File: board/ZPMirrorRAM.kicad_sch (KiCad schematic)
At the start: 17 parts, among them IC1 74LS189, IC2 74LS189, IC3 74LS189, IC4 SN74LS189AN, U13 74F08, U24 74F20, U25 74F02, U26 74LS154, U27 74HC138

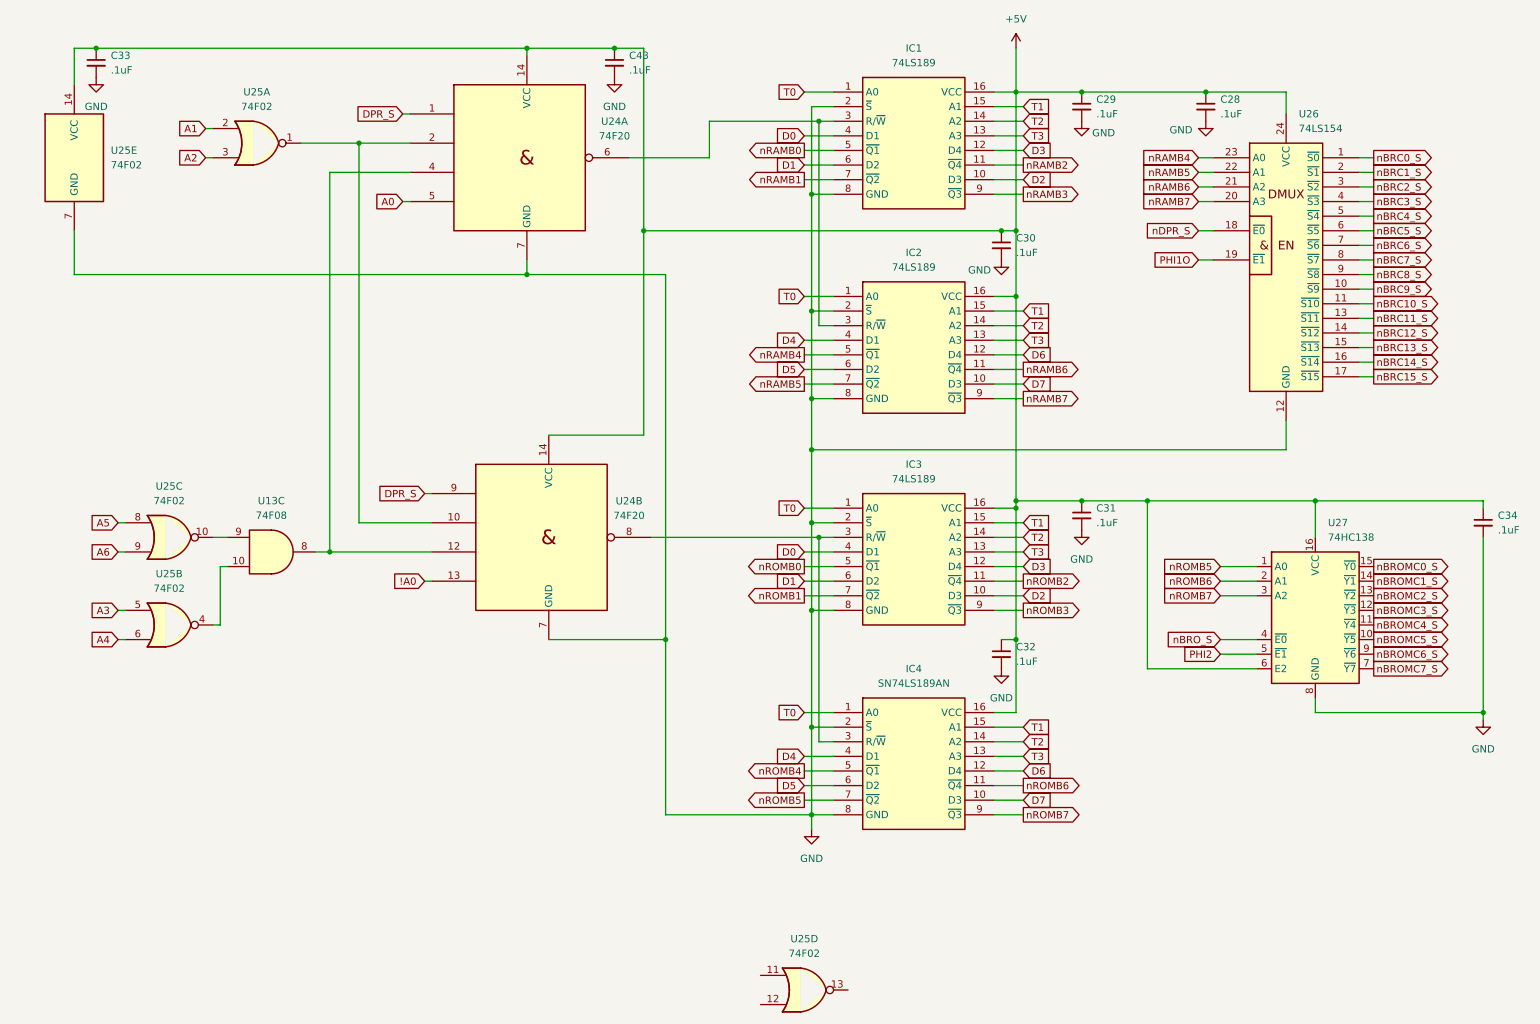
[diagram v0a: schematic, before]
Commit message: Fixing pin assignments
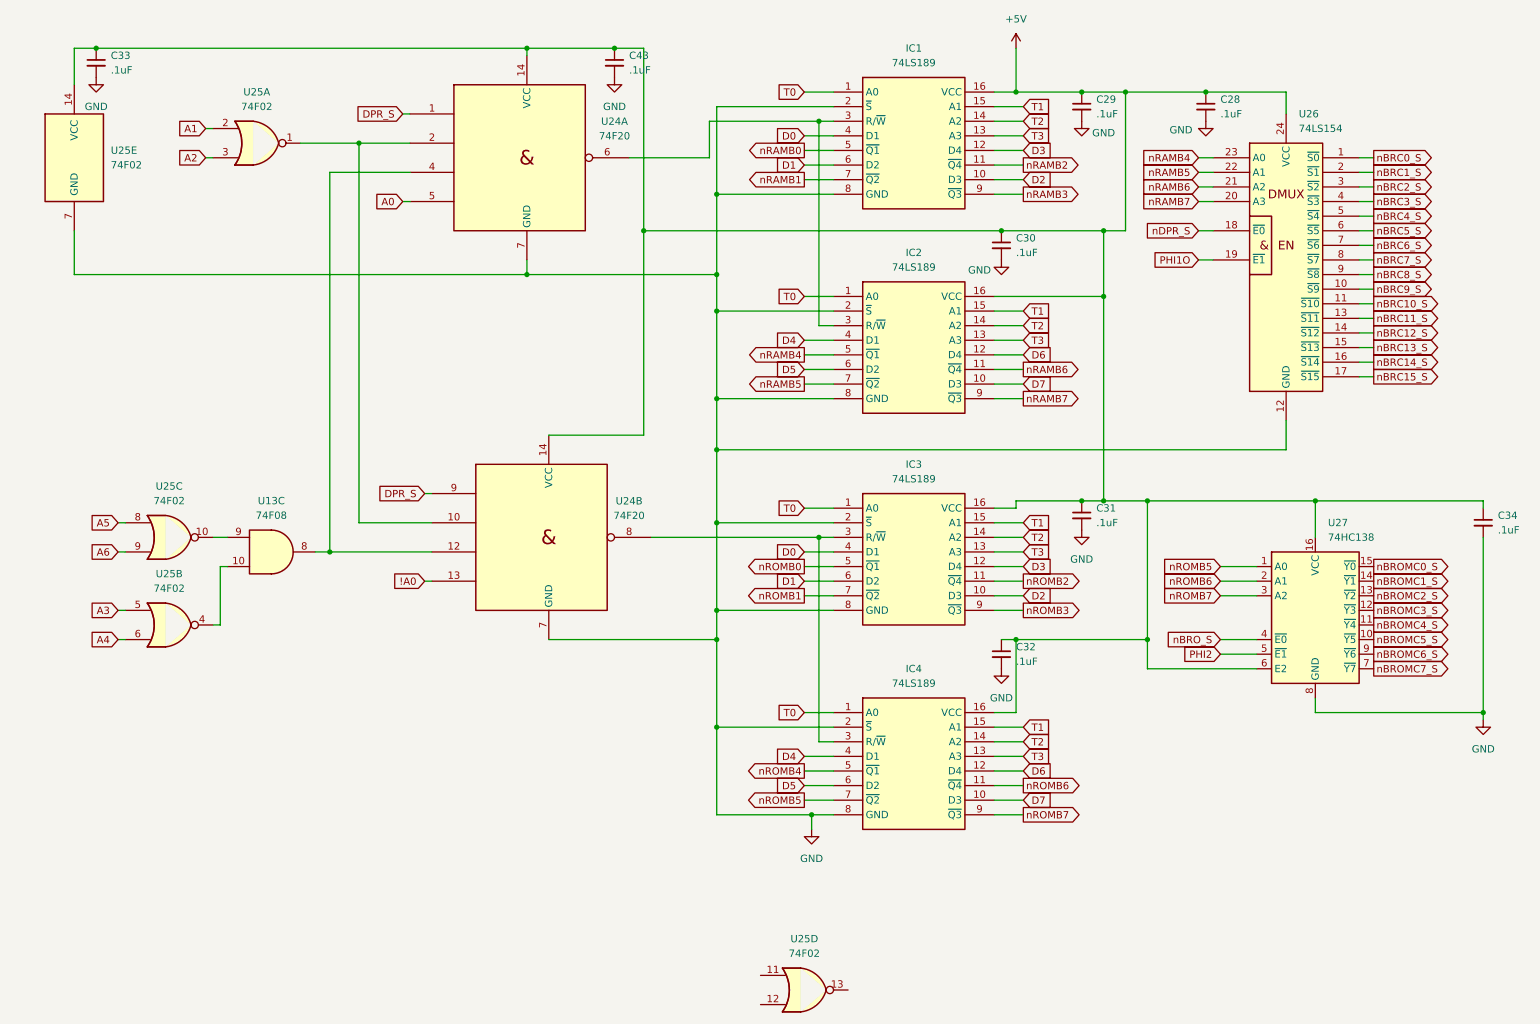
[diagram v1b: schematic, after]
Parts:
- IC4: value SN74LS189AN -> 74LS189

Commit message: Added surface mount version of memory daughter cards, and lots of schematic updates and fixes, including adding dedicated registers for shared memory bank select at $FFF1 and IRQ vTable entry selector at $FFF2 along with the IRQ vTable registers and priority encoders for 16 IRQs
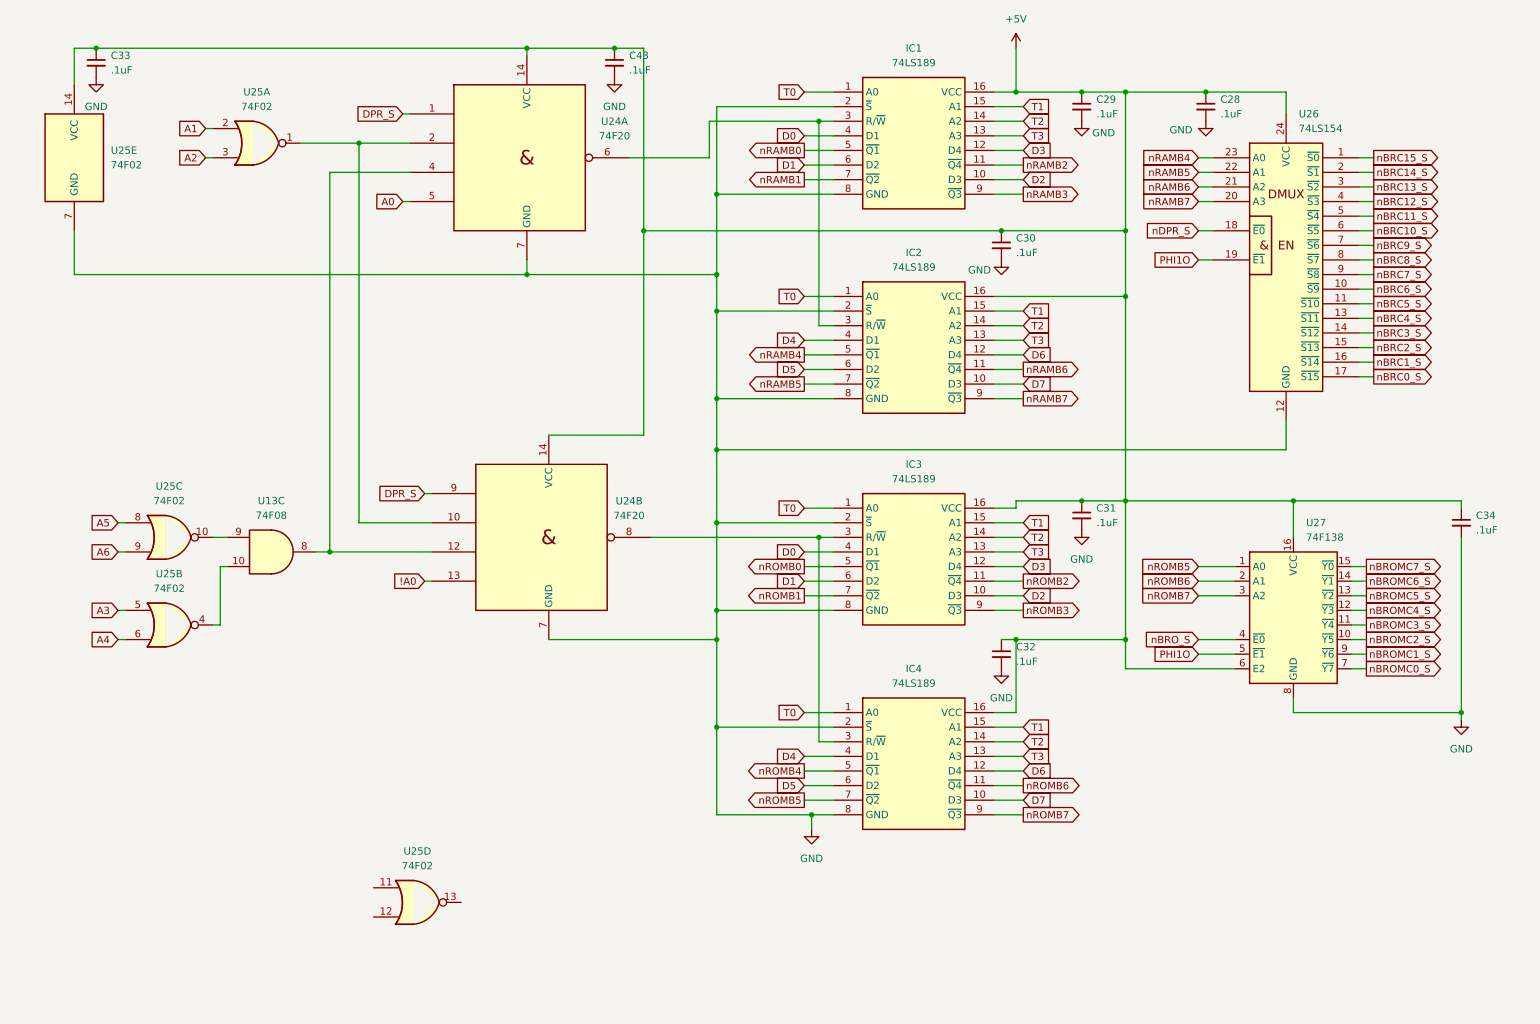
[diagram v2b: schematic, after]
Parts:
- U27: value 74HC138 -> 74F138
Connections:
- net PHI2 is gone; now on net PHI1O: U27.5 (~{E1})
- net nBRC0_S: now also U26.17 (~{S15}); no longer U26.1 (~{S0})
- net nBRC10_S: now also U26.6 (~{S5}); no longer U26.11 (~{S10})
- net nBRC11_S: now also U26.5 (~{S4}); no longer U26.13 (~{S11})
- net nBRC12_S: now also U26.4 (~{S3}); no longer U26.14 (~{S12})
- net nBRC13_S: now also U26.3 (~{S2}); no longer U26.15 (~{S13})
- net nBRC14_S: now also U26.2 (~{S1}); no longer U26.16 (~{S14})
- net nBRC15_S: now also U26.1 (~{S0}); no longer U26.17 (~{S15})
- net nBRC1_S: now also U26.16 (~{S14}); no longer U26.2 (~{S1})
- net nBRC2_S: now also U26.15 (~{S13}); no longer U26.3 (~{S2})
- net nBRC3_S: now also U26.14 (~{S12}); no longer U26.4 (~{S3})
- net nBRC4_S: now also U26.13 (~{S11}); no longer U26.5 (~{S4})
- net nBRC5_S: now also U26.11 (~{S10}); no longer U26.6 (~{S5})
- net nBRC6_S: now also U26.10 (~{S9}); no longer U26.7 (~{S6})
- net nBRC7_S: now also U26.9 (~{S8}); no longer U26.8 (~{S7})
- net nBRC8_S: now also U26.8 (~{S7}); no longer U26.9 (~{S8})
- net nBRC9_S: now also U26.7 (~{S6}); no longer U26.10 (~{S9})
- net nBROMC0_S: now also U27.7 (~{Y7}); no longer U27.15 (~{Y0})
- net nBROMC1_S: now also U27.9 (~{Y6}); no longer U27.14 (~{Y1})
- net nBROMC2_S: now also U27.10 (~{Y5}); no longer U27.13 (~{Y2})
- net nBROMC3_S: now also U27.11 (~{Y4}); no longer U27.12 (~{Y3})
- net nBROMC4_S: now also U27.12 (~{Y3}); no longer U27.11 (~{Y4})
- net nBROMC5_S: now also U27.13 (~{Y2}); no longer U27.10 (~{Y5})
- net nBROMC6_S: now also U27.14 (~{Y1}); no longer U27.9 (~{Y6})
- net nBROMC7_S: now also U27.15 (~{Y0}); no longer U27.7 (~{Y7})
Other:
- moved on the sheet: C34, U27

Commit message: More main PCB updates.  Rearranged some things.  Bypass caps near PS connector.  Moved front panel connector to opposite side of board.
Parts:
- IC1, IC2, IC3, IC4: footprint Package_DIP:DIP-16_W7.62mm_LongPads -> Package_DIP:DIP-16_W7.62mm_Socket_LongPads
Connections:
- net nDPR_S renamed nBRA_S
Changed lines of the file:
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@@
 		)
 	)
-	(global_label "nDPR_S"
+	(global_label "nBRA_S"
 		(shape input)
 		(at 223.52 52.07 180)
@@
 		)
 		(property "Intersheetrefs" "${INTERSHEET_REFS}"
-			(at 213.3987 52.07 0)
+			(at 213.5801 52.07 0)
 			(effects
 				(font
@@
 			)
 		)
-		(property "Footprint" "Package_DIP:DIP-16_W7.62mm_LongPads"
+		(property "Footprint" "Package_DIP:DIP-16_W7.62mm_Socket_LongPads"
 			(at 184.15 158.42 0)
 			(effects
@@
 			)
 		)
-		(property "Footprint" "Package_DIP:DIP-16_W7.62mm_LongPads"
+		(property "Footprint" "Package_DIP:DIP-16_W7.62mm_Socket_LongPads"
 			(at 184.15 122.86 0)
 			(effects
@@
 			)
 		)
-		(property "Footprint" "Package_DIP:DIP-16_W7.62mm_LongPads"
+		(property "Footprint" "Package_DIP:DIP-16_W7.62mm_Socket_LongPads"
 			(at 184.15 230.81 0)
 			(effects
@@
 			)
 		)
-		(property "Footprint" "Package_DIP:DIP-16_W7.62mm_LongPads"
+		(property "Footprint" "Package_DIP:DIP-16_W7.62mm_Socket_LongPads"
 			(at 184.15 195.25 0)
 			(effects

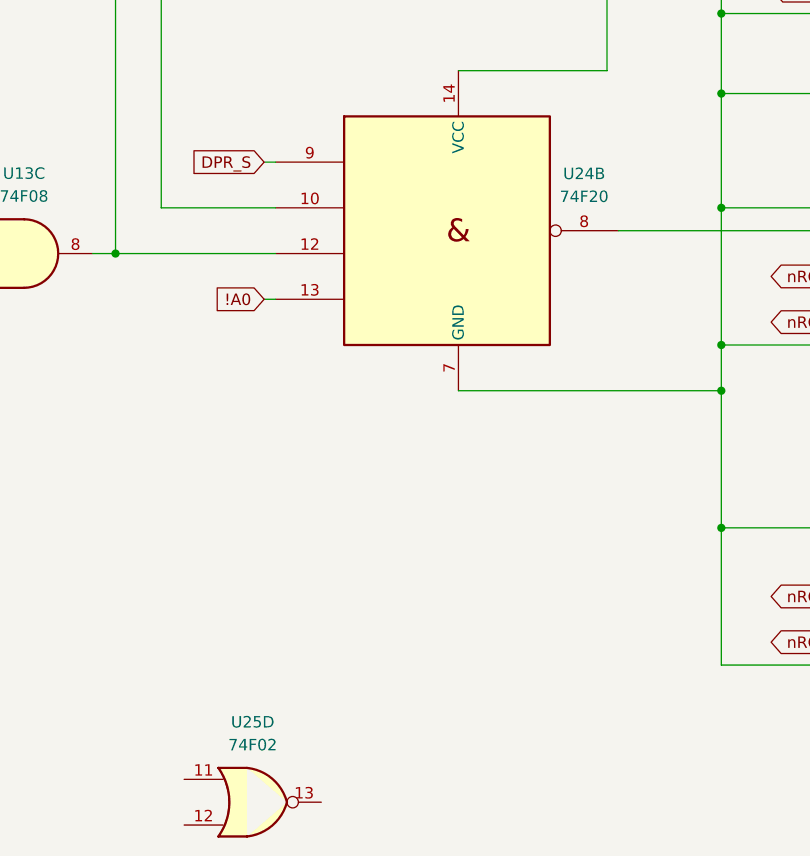
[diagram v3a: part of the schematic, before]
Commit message: Latest main PCB update with FFF1 and FFF2 added and decode logic updated to exclude FFFE and FFFF in nOSROM_S signal
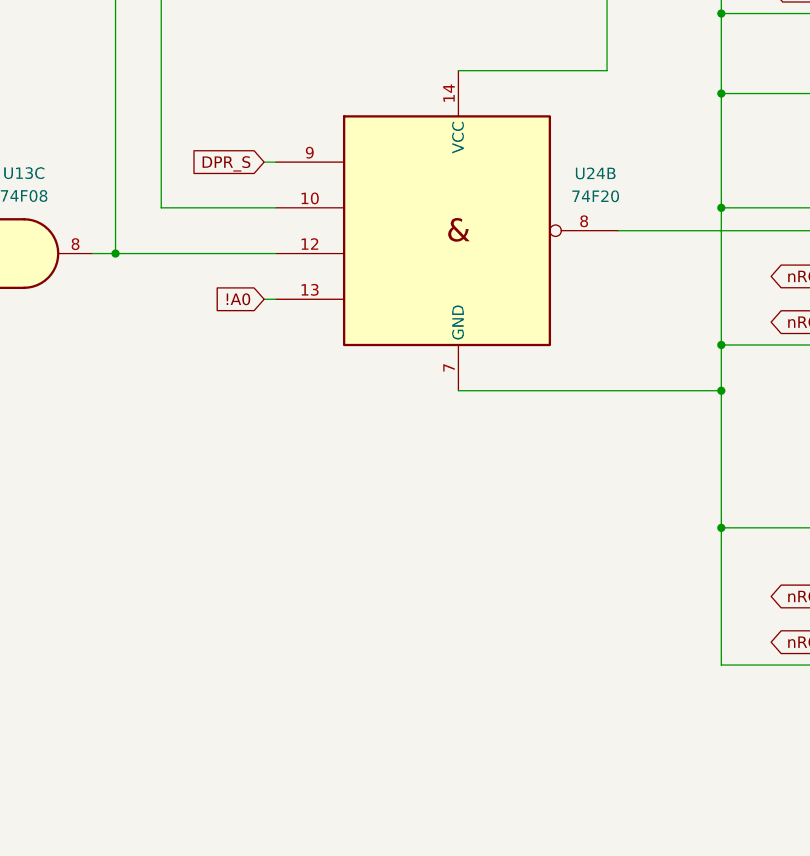
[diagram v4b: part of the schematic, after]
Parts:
- removed unit 4 of U25
- U13, U24, U25: footprint Package_DIP:DIP-14_W7.62mm_LongPads -> Package_DIP:DIP-14_W7.62mm_Socket_LongPads
- U26: footprint Package_DIP:DIP-24_W15.24mm_LongPads -> Package_DIP:DIP-24_W15.24mm_Socket_LongPads
- U27: footprint Package_DIP:DIP-16_W7.62mm_LongPads -> Package_DIP:DIP-16_W7.62mm_Socket_LongPads
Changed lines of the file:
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@@
 			)
 		)
-		(property "Footprint" "Package_DIP:DIP-16_W7.62mm_LongPads"
+		(property "Footprint" "Package_DIP:DIP-16_W7.62mm_Socket_LongPads"
 			(at 240.03 120.65 0)
 			(effects
@@
 		(fields_autoplaced yes)
 		(property "Reference" "U24"
-			(at 124.46 99.0914 0)
+			(at 125.73 99.0914 0)
 			(effects
 				(font
@@
 		)
 		(property "Value" "74F20"
-			(at 124.46 101.6314 0)
-			(effects
-				(font
-					(size 1.27 1.27)
-				)
-			)
-		)
-		(property "Footprint" "Package_DIP:DIP-14_W7.62mm_LongPads"
+			(at 125.73 101.6314 0)
+			(effects
+				(font
+					(size 1.27 1.27)
+				)
+			)
+		)
+		(property "Footprint" "Package_DIP:DIP-14_W7.62mm_Socket_LongPads"
 			(at 110.49 105.41 0)
 			(effects
@@
 			)
 		)
-		(property "Footprint" "Package_DIP:DIP-14_W7.62mm_LongPads"
+		(property "Footprint" "Package_DIP:DIP-14_W7.62mm_Socket_LongPads"
 			(at 44.45 105.41 0)
 			(effects
@@
 			)
 		)
-		(property "Footprint" "Package_DIP:DIP-14_W7.62mm_LongPads"
+		(property "Footprint" "Package_DIP:DIP-14_W7.62mm_Socket_LongPads"
 			(at 106.68 39.37 0)
 			(effects
@@
 			)
 		)
-		(property "Footprint" "Package_DIP:DIP-14_W7.62mm_LongPads"
+		(property "Footprint" "Package_DIP:DIP-14_W7.62mm_Socket_LongPads"
 			(at 44.45 120.65 0)
 			(effects
@@
 			)
 		)
-		(property "Footprint" "Package_DIP:DIP-24_W15.24mm_LongPads"
+		(property "Footprint" "Package_DIP:DIP-24_W15.24mm_Socket_LongPads"
 			(at 238.76 59.69 0)
 			(effects
@@
 					(reference "U26")
 					(unit 1)
-				)
-			)
-		)
-	)
-	(symbol
-		(lib_id "74xx:7402")
-		(at 87.63 168.91 0)
-		(unit 4)
-		(exclude_from_sim no)
-		(in_bom yes)
-		(on_board yes)
-		(dnp no)
-		(fields_autoplaced yes)
-		(property "Reference" "U25"
-			(at 87.63 160.02 0)
-			(effects
-				(font
-					(size 1.27 1.27)
-				)
-			)
-		)
-		(property "Value" "74F02"
-			(at 87.63 162.56 0)
-			(effects
-				(font
-					(size 1.27 1.27)
-				)
-			)
-		)
-		(property "Footprint" "Package_DIP:DIP-14_W7.62mm_LongPads"
-			(at 87.63 168.91 0)
-			(effects
-				(font
-					(size 1.27 1.27)
-				)
-				(hide yes)
-			)
-		)
-		(property "Datasheet" "http://www.ti.com/lit/gpn/sn7402"
-			(at 87.63 168.91 0)
-			(effects
-				(font
-					(size 1.27 1.27)
-				)
-				(hide yes)
-			)
-		)
-		(property "Description" "quad 2-input NOR gate"
-			(at 87.63 168.91 0)
-			(effects
-				(font
-					(size 1.27 1.27)
-				)
-				(hide yes)
-			)
-		)
-		(pin "10"
-		)
-		(pin "2"
-		)
-		(pin "12"
-		)
-		(pin "9"
-		)
-		(pin "13"
-		)
-		(pin "8"
-		)
-		(pin "6"
-		)
-		(pin "4"
-		)
-		(pin "5"
-		)
-		(pin "11"
-		)
-		(pin "14"
-		)
-		(pin "1"
-		)
-		(pin "7"
-		)
-		(pin "3"
-		)
-		(instances
-			(project "hydra-16"
-				(path "/ef29fc71-3fec-48b5-8a1a-46bee537a98c/b525633b-f72d-4f83-aa63-6fabb8850756"
-					(reference "U25")
-					(unit 4)
 				)
 			)
@@
 			)
 		)
-		(property "Footprint" "Package_DIP:DIP-14_W7.62mm_LongPads"
+		(property "Footprint" "Package_DIP:DIP-14_W7.62mm_Socket_LongPads"
 			(at 27.94 39.37 0)
 			(effects
@@
 			)
 		)
-		(property "Footprint" "Package_DIP:DIP-14_W7.62mm_LongPads"
+		(property "Footprint" "Package_DIP:DIP-14_W7.62mm_Socket_LongPads"
 			(at 62.23 107.95 0)
 			(effects
@@
 			)
 		)
-		(property "Footprint" "Package_DIP:DIP-14_W7.62mm_LongPads"
+		(property "Footprint" "Package_DIP:DIP-14_W7.62mm_Socket_LongPads"
 			(at 59.69 36.83 0)
 			(effects
